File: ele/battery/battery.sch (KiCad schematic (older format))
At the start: 31 parts, among them J1 banana, J10 B1_trans, J11 B2_trans, J12 B1_M, J13 B2_P, J14 mech, J15 mech, J16 B1_P_tans_b, J17 B1_M_tans_b, J18 B2_P_tans_b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

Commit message: ele: battery - add voltage/state LED indicators
Use this buttons:
- https://www.tme.eu/cz/details/tactb-64k-f/mikrospinace-tact/ninigi/
- https://www.aliexpress.com/item/50PCS-LOT-SMD-4-4-1-5MM-7MM-4X4X1-5MM-7MM-5-2mm-x-5-2mm/32907185072.html
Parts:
- added D1, D2: LED_RED, LED_SMD:LED_1206_3216Metric_Pad1.42x1.75mm_HandSolder, symbol Device:LED
- added D3, D4: D_Zener_2V, Diode_SMD:D_1206_3216Metric_Pad1.42x1.75mm_HandSolder, symbol Device:D_Zener
- added R1, R2: R, Resistor_SMD:R_1206_3216Metric_Pad1.42x1.75mm_HandSolder, symbol Device:R
- added SW1, SW2: SW_Push, Button_Switch_SMD:SW_SPST_EVQP0, symbol Switch:SW_Push
- U1, U2: symbol yaqwsx:ChinaLiIonCharger -> battery-rescue:ChinaLiIonCharger-yaqwsx
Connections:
- wire segments 30 -> 46
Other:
- moved on the sheet: J16, J17, J18, J19, J20, J21, J22, J23, J24, J25, J26, J27

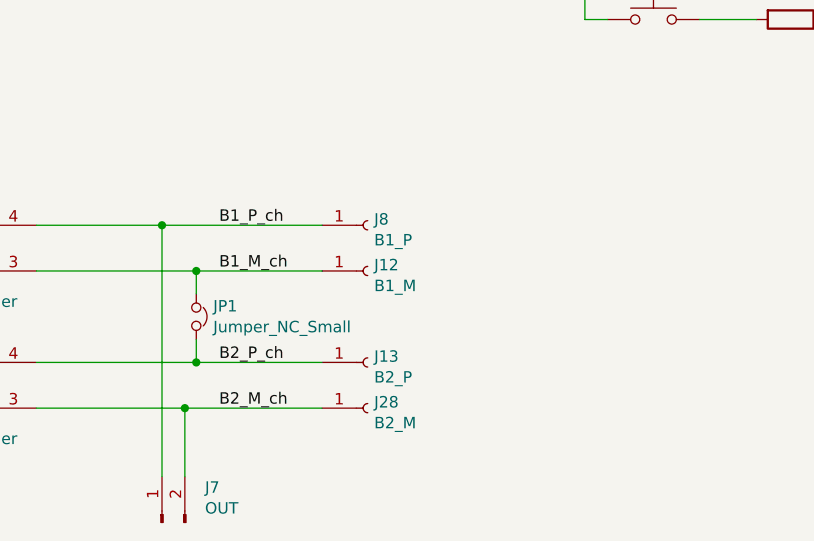
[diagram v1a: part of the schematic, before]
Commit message: ele: battery - add balancer connector
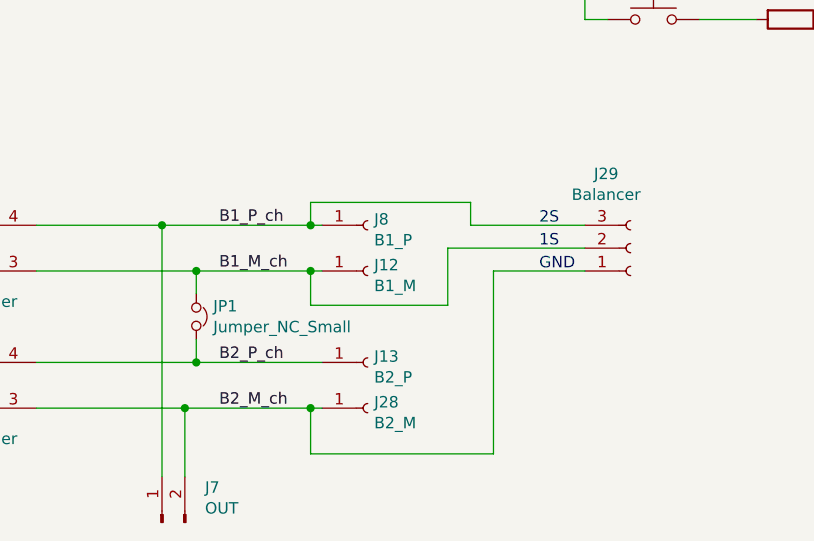
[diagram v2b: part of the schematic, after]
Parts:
- added J29: Balancer, Connector_PinSocket_2.54mm:PinSocket_1x03_P2.54mm_Horizontal, symbol Connector:Conn_01x03_Female
- J7: footprint yaqwsx:2_pads_5mm -> BATTERY:2_pads_5mm
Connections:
- net B1_M_ch: now also J29.2 (Pin_2)
- net B1_P_ch: now also J29.3 (Pin_3)
- net B2_M_ch: now also J29.1 (Pin_1)
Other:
- note added: "1S"
- note added: "2S"
- note added: "GND"
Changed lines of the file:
@@
 EESchema Schematic File Version 4
 LIBS:battery-cache
-EELAYER 26 0
+EELAYER 29 0
 EELAYER END
 $Descr A4 11693 8268
@@
 $EndComp
 Wire Wire Line
-	5350 4100 4650 4100
+	5350 4100 5300 4100
 Wire Wire Line
 	4100 4300 4800 4300
@@
 F 0 "J7" V 4803 5212 50  0000 R CNN
 F 1 "OUT" V 4712 5212 50  0000 R CNN
-F 2 "yaqwsx:2_pads_5mm" H 4650 5400 50  0001 C CNN
+F 2 "BATTERY:2_pads_5mm" H 4650 5400 50  0001 C CNN
 F 3 "~" H 4650 5400 50  0001 C CNN
 	1    4650 5400
@@
 Connection ~ 4750 4900
 Wire Wire Line
-	4750 4900 5350 4900
+	4750 4900 5300 4900
 $Comp
 L Device:Jumper_NC_Small JP1
@@
 Connection ~ 4800 4300
 Wire Wire Line
-	4800 4300 5350 4300
+	4800 4300 5300 4300
 Wire Wire Line
 	4800 4600 4800 4700
@@
 Wire Wire Line
 	7550 3200 8100 3200
+Wire Wire Line
+	5300 4900 5300 5100
+Wire Wire Line
+	5300 5100 6100 5100
+Wire Wire Line
+	6100 4300 6500 4300
+Connection ~ 5300 4900
+Wire Wire Line
+	5300 4900 5350 4900
+Wire Wire Line
+	5300 4300 5300 4450
+Wire Wire Line
+	5300 4450 5900 4450
+Wire Wire Line
+	5900 4450 5900 4200
+Wire Wire Line
+	5900 4200 6500 4200
+Connection ~ 5300 4300
+Wire Wire Line
+	5300 4300 5350 4300
+Wire Wire Line
+	5300 4100 5300 4000
+Wire Wire Line
+	5300 4000 6000 4000
+Connection ~ 5300 4100
+Wire Wire Line
+	5300 4100 4650 4100
+$Comp
+L Connector:Conn_01x03_Female J29
+U 1 1 5CA69FC1
+P 6700 4200
+F 0 "J29" H 6593 3875 50  0000 C CNN
+F 1 "Balancer" H 6593 3966 50  0000 C CNN
+F 2 "Connector_PinSocket_2.54mm:PinSocket_1x03_P2.54mm_Horizontal" H 6700 4200 50  0001 C CNN
+F 3 "~" H 6700 4200 50  0001 C CNN
+	1    6700 4200
+	1    0    0    1
+$EndComp
+Wire Wire Line
+	6100 4300 6100 5100
+Wire Wire Line
+	6000 4100 6500 4100
+Wire Wire Line
+	6000 4000 6000 4100
+Text Notes 6300 4300 0    50   ~ 0
+GND
+Text Notes 6300 4200 0    50   ~ 0
+1S
+Text Notes 6300 4100 0    50   ~ 0
+2S
 $EndSCHEMATC

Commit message: ele: Change battery outline
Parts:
- added J30: mech, BATTERY:pad_3x5, symbol Connector:Conn_01x01_Male
- J9: footprint yaqwsx:pad_3x5 -> BATTERY:pad_3x5
- U1: footprint yaqwsx:LiOnCharger -> battery:LiOnCharger; symbol battery-rescue:ChinaLiIonCharger-yaqwsx -> battery:ChinaLiIonCharger
- U2: symbol battery-rescue:ChinaLiIonCharger-yaqwsx -> battery:ChinaLiIonCharger
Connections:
- no-connect marks 3 -> 4
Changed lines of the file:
@@
 F 0 "J9" H 4523 1080 50  0000 R CNN
 F 1 "mech" H 4523 1171 50  0000 R CNN
-F 2 "yaqwsx:pad_3x5" H 4550 1150 50  0001 C CNN
+F 2 "BATTERY:pad_3x5" H 4550 1150 50  0001 C CNN
 F 3 "~" H 4550 1150 50  0001 C CNN
 	1    4550 1150
@@
 B2-
 $Comp
-L battery-rescue:ChinaLiIonCharger-yaqwsx U1
+L battery:ChinaLiIonCharger U1
 U 1 1 5C13AEE9
 P 3700 4200
 F 0 "U1" H 3700 4525 50  0000 C CNN
 F 1 "ChinaLiIonCharger" H 3700 4434 50  0000 C CNN
-F 2 "yaqwsx:LiOnCharger" H 3700 4200 50  0001 C CNN
+F 2 "battery:LiOnCharger" H 3700 4200 50  0001 C CNN
 F 3 "" H 3700 4200 50  0001 C CNN
 	1    3700 4200
@@
 $EndComp
 $Comp
-L battery-rescue:ChinaLiIonCharger-yaqwsx U2
+L battery:ChinaLiIonCharger U2
 U 1 1 5C13AF67
 P 3700 4800
@@
 Text Notes 6300 4100 0    50   ~ 0
 2S
+$Comp
+L Connector:Conn_01x01_Male J30
+U 1 1 5CA7C8EA
+P 4550 1400
+F 0 "J30" H 4523 1330 50  0000 R CNN
+F 1 "mech" H 4523 1421 50  0000 R CNN
+F 2 "BATTERY:pad_3x5" H 4550 1400 50  0001 C CNN
+F 3 "~" H 4550 1400 50  0001 C CNN
+	1    4550 1400
+	-1   0    0    1
+$EndComp
+NoConn ~ 4350 1400
 $EndSCHEMATC

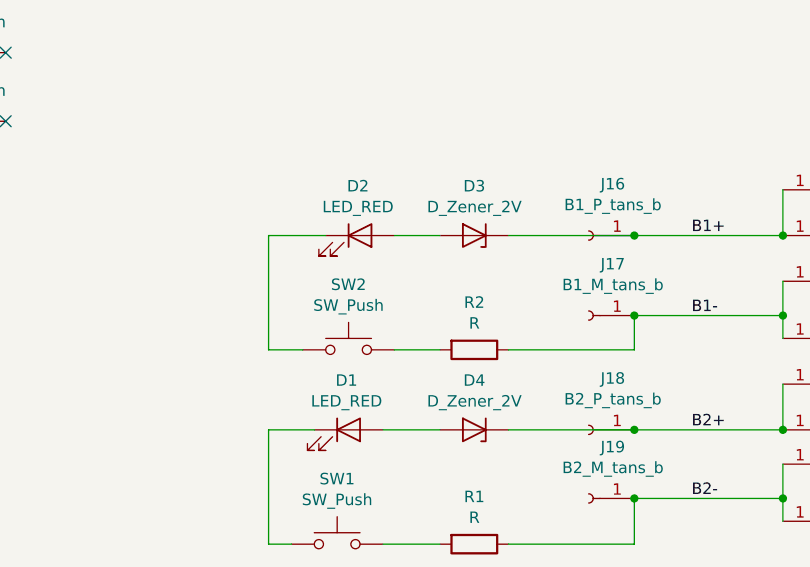
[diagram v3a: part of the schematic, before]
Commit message: ele: battery - improve battery indicator
- rename LEDs and diodes
- add missing routes on switch
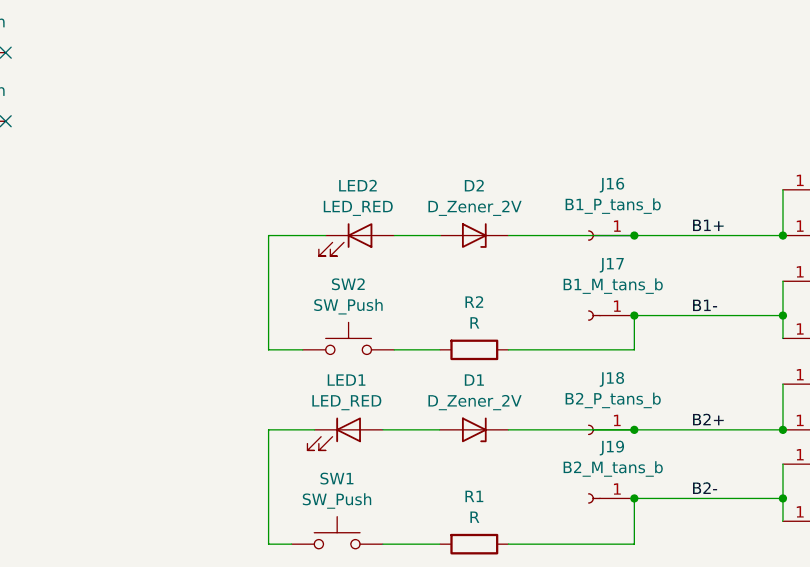
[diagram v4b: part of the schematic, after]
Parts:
- renumbered D4 to D1, D3 to D2, D1 to LED1, D2 to LED2
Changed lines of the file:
@@
 B2_M_ch
 $Comp
-L Device:LED D1
+L Device:LED LED1
 U 1 1 5CA4BABE
 P 6850 2700
-F 0 "D1" H 6841 2916 50  0000 C CNN
+F 0 "LED1" H 6841 2916 50  0000 C CNN
 F 1 "LED_RED" H 6841 2825 50  0000 C CNN
 F 2 "LED_SMD:LED_1206_3216Metric_Pad1.42x1.75mm_HandSolder" H 6850 2700 50  0001 C CNN
@@
 $EndComp
 $Comp
-L Device:D_Zener D4
+L Device:D_Zener D1
 U 1 1 5CA4BCEC
 P 7400 2700
-F 0 "D4" H 7400 2484 50  0000 C CNN
+F 0 "D1" H 7400 2484 50  0000 C CNN
 F 1 "D_Zener_2V" H 7400 2575 50  0000 C CNN
 F 2 "Diode_SMD:D_1206_3216Metric_Pad1.42x1.75mm_HandSolder" H 7400 2700 50  0001 C CNN
@@
 Connection ~ 8100 2700
 $Comp
-L Device:LED D2
+L Device:LED LED2
 U 1 1 5CA52B33
 P 6900 1850
-F 0 "D2" H 6891 2066 50  0000 C CNN
+F 0 "LED2" H 6891 2066 50  0000 C CNN
 F 1 "LED_RED" H 6891 1975 50  0000 C CNN
 F 2 "LED_SMD:LED_1206_3216Metric_Pad1.42x1.75mm_HandSolder" H 6900 1850 50  0001 C CNN
@@
 $EndComp
 $Comp
-L Device:D_Zener D3
+L Device:D_Zener D2
 U 1 1 5CA52BB9
 P 7400 1850
-F 0 "D3" H 7400 1634 50  0000 C CNN
+F 0 "D2" H 7400 1634 50  0000 C CNN
 F 1 "D_Zener_2V" H 7400 1725 50  0000 C CNN
 F 2 "Diode_SMD:D_1206_3216Metric_Pad1.42x1.75mm_HandSolder" H 7400 1850 50  0001 C CNN

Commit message: ele: Fix symbol and footprint libraries
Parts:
- J7: footprint BATTERY:2_pads_5mm -> RB3201:2_pads_5mm
- U1: footprint battery:LiOnCharger -> RB3201:LiOnCharger; symbol battery:ChinaLiIonCharger -> RB3201:ChinaLiIonCharger
- U2: footprint yaqwsx:LiOnCharger -> RB3201:LiOnCharger; symbol battery:ChinaLiIonCharger -> RB3201:ChinaLiIonCharger
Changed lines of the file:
@@
 B2-
 $Comp
-L battery:ChinaLiIonCharger U1
+L RB3201:ChinaLiIonCharger U1
 U 1 1 5C13AEE9
 P 3700 4200
 F 0 "U1" H 3700 4525 50  0000 C CNN
 F 1 "ChinaLiIonCharger" H 3700 4434 50  0000 C CNN
-F 2 "battery:LiOnCharger" H 3700 4200 50  0001 C CNN
+F 2 "RB3201:LiOnCharger" H 3700 4200 50  0001 C CNN
 F 3 "" H 3700 4200 50  0001 C CNN
 	1    3700 4200
@@
 $EndComp
 $Comp
-L battery:ChinaLiIonCharger U2
+L RB3201:ChinaLiIonCharger U2
 U 1 1 5C13AF67
 P 3700 4800
 F 0 "U2" H 3700 5125 50  0000 C CNN
 F 1 "ChinaLiIonCharger" H 3700 5034 50  0000 C CNN
-F 2 "yaqwsx:LiOnCharger" H 3700 4800 50  0001 C CNN
+F 2 "RB3201:LiOnCharger" H 3700 4800 50  0001 C CNN
 F 3 "" H 3700 4800 50  0001 C CNN
 	1    3700 4800
@@
 F 0 "J7" V 4803 5212 50  0000 R CNN
 F 1 "OUT" V 4712 5212 50  0000 R CNN
-F 2 "BATTERY:2_pads_5mm" H 4650 5400 50  0001 C CNN
+F 2 "RB3201:2_pads_5mm" H 4650 5400 50  0001 C CNN
 F 3 "~" H 4650 5400 50  0001 C CNN
 	1    4650 5400
